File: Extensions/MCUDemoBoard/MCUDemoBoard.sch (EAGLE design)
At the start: 23 parts, among them J1 CONN_20X2NOSILK, SW1 SPST_TACT-KMR2, U1 ATSAMD21J18A-AUT, U6 MAX3232, X4 NX3215SA-32.768K-STD-MUA-8

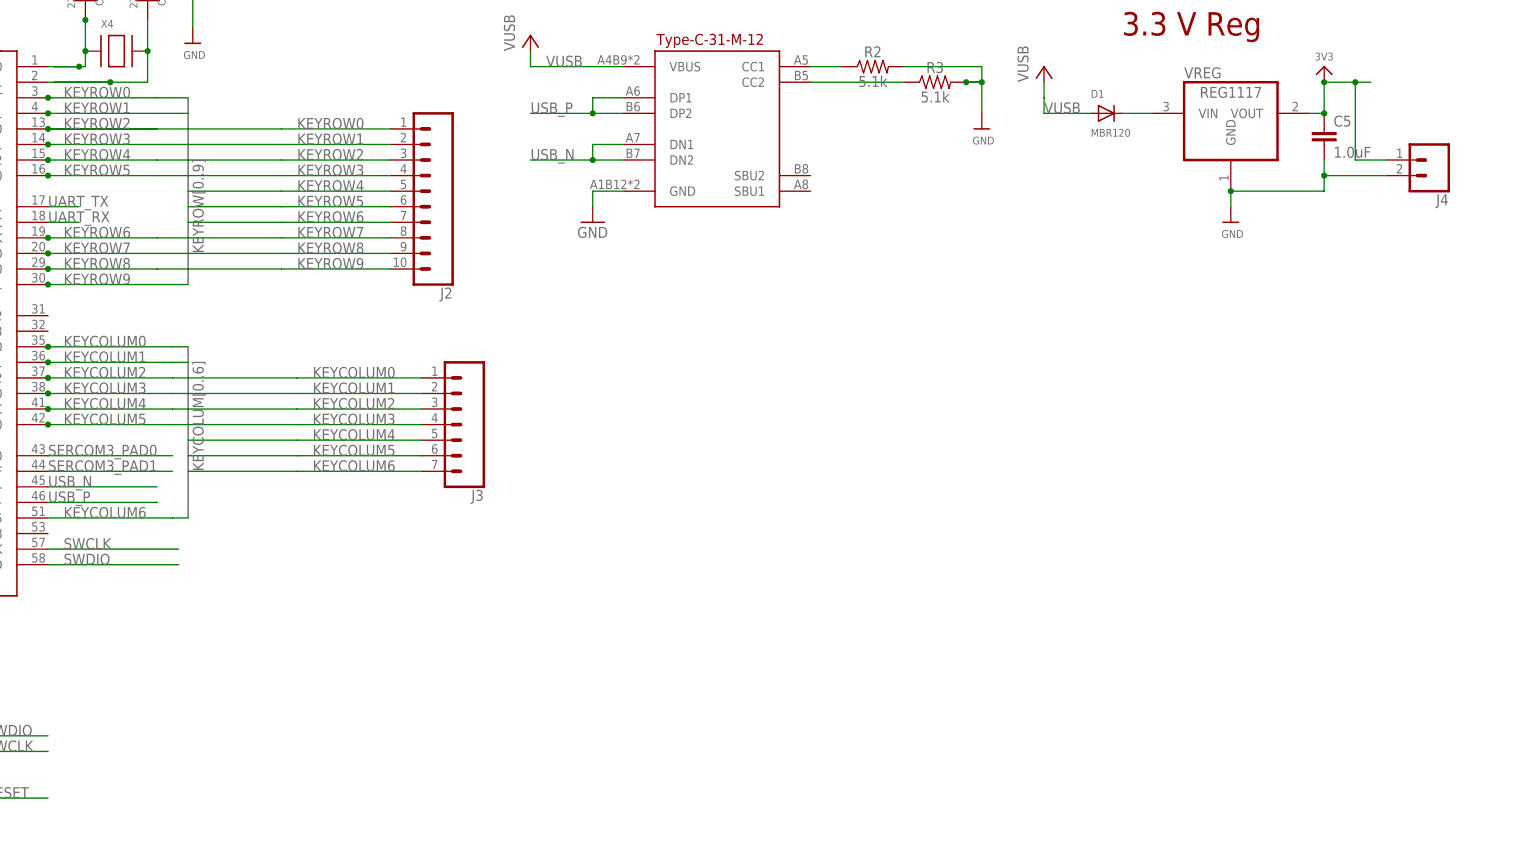
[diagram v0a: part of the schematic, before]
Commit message: changed MCU test board for FPC cable, other mods, moved test keyboard
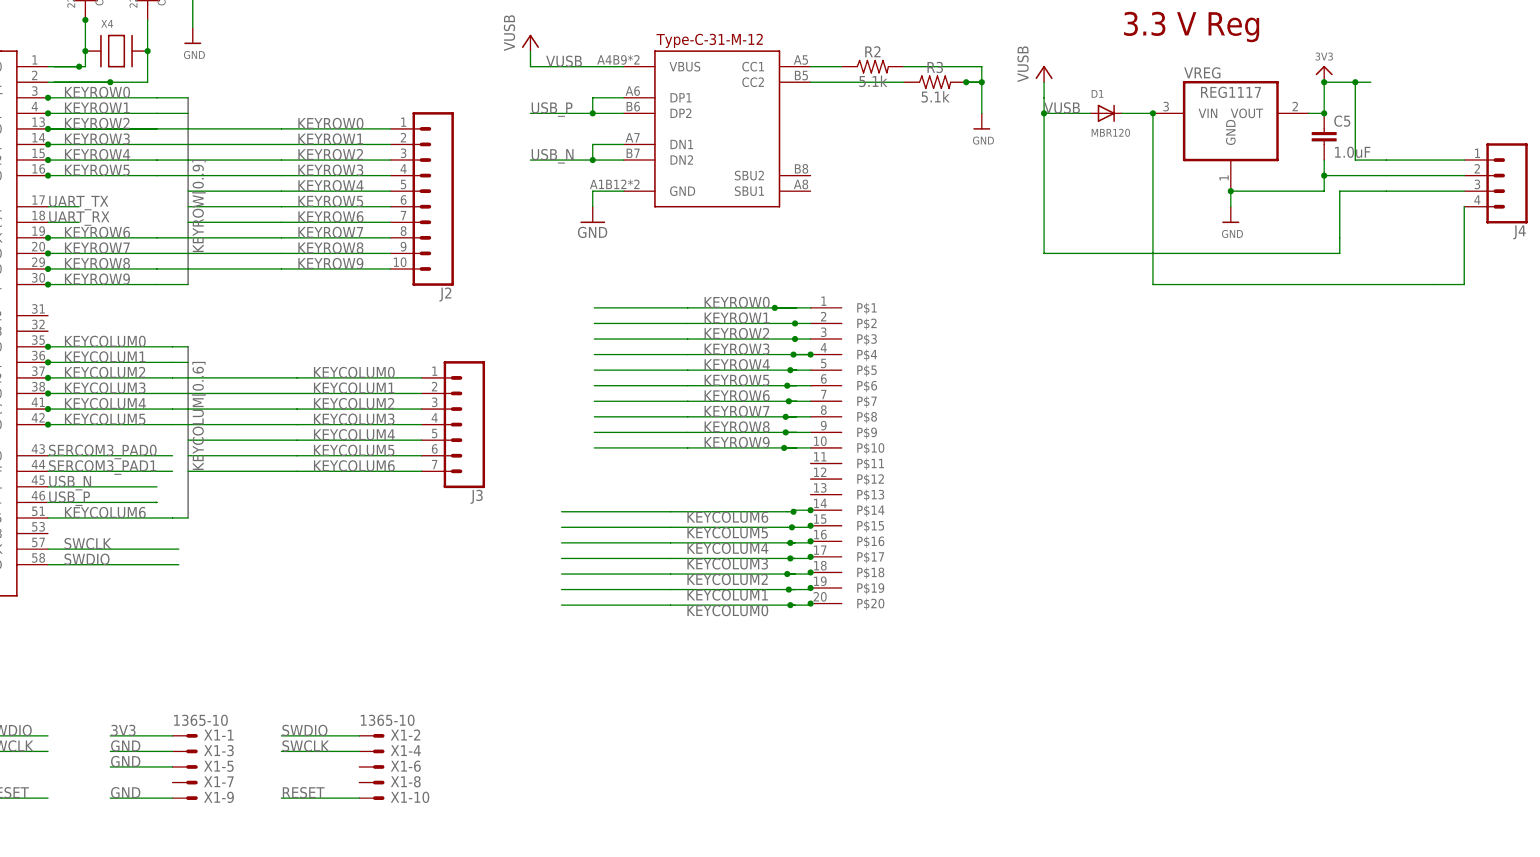
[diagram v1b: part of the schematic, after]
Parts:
- added U$1: FC1-20-L2-T-WT20PIN, FPC:FC1-20-L2-T-WT20PIN
- added X1: 1365-10, con-leotronics:1365-10
- J4: device SparkFun-Connectors:CONN_02 -> SparkFun-Connectors:CONN_04
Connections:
- net 3V3: now also X1-1.S
- net GND: now also X1-3.S, X1-5.S, X1-9.S
- net KEYCOLUM0: now also U$1.P$20
- net KEYCOLUM1: now also U$1.P$19
- net KEYCOLUM2: now also U$1.P$18
- net KEYCOLUM3: now also U$1.P$17
- net KEYCOLUM4: now also U$1.P$16
- net KEYCOLUM5: now also U$1.P$15
- net KEYCOLUM6: now also U$1.P$14
- net KEYROW0: now also U$1.P$1
- net KEYROW1: now also U$1.P$2
- net KEYROW2: now also U$1.P$3
- net KEYROW3: now also U$1.P$4
- net KEYROW4: now also U$1.P$5
- net KEYROW5: now also U$1.P$6
- net KEYROW6: now also U$1.P$7
- net KEYROW7: now also U$1.P$8
- net KEYROW8: now also U$1.P$9
- net KEYROW9: now also U$1.P$10
- net N$2: now also J4.4
- net RESET: now also X1-10.S
- net SWCLK: now also X1-4.S
- net SWDIO: now also X1-2.S
- net VUSB: now also J4.3

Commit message: Added SamD51 demo board; tried to get D51 software working
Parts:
- removed C12: 1.0uF, SparkFun-Capacitors:1.0UF-0805-25V-10%
- removed C26, C27: 22pF, SparkFun-Capacitors:1.0UF-0805-25V-10%
- removed D1: MBR120, adafruit:DIODE_SOD-123FL
- removed SW1: SPST_TACT-KMR2, adafruit:SPST_TACT-KMR2
- removed U1: ATSAMD21J18A-AUT, ATSam21:ATSAMD21J18A-AUT
- removed X4: NX3215SA-32.768K-STD-MUA-8, adafruit2:XTAL-3.2X1.5
- added C1, C2: 22pF, SparkFun-Capacitors:1.0UF-0805-25V-10%
- added C14: 10uF, microbuilder:CAP_CERAMIC0805-NOOUTLINE
- added C15: 1uF, microbuilder:CAP_CERAMIC0603_NO
- added C16, C17, C18, C19, C20, C21, C25, C28, C29, C30, C31: .1u, microbuilder:CAP_CERAMIC0603_NO
- added IC1: ATSAMD51N19A-AU, SamacSys_Parts:ATSAMD51N19A-AU
- added L3: 10uH, microbuilder:INDUCTOR
- added R15: 10K, microbuilder:RESISTOR_0603_NOOUT
- added SW2: SPST_TACT-KMR2, adafruit:SPST_TACT-KMR2
- added X2: NX3215SA-32.768K-STD-MUA-8, adafruit2:XTAL-3.2X1.5
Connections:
- removed net N$2: D1.C, J4.4, VREG.VIN
- removed net N$3: C12.1, U1.VDDCORE
- removed net N$54: C26.1, U1.PA00/EINT0/SERCOM1.0, X4.P$1
- removed net N$55: C27.1, U1.PA01/EINT1/SERCOM1.1, X4.P$2
- removed net PB31: U1.PB31
- removed net SERCOM3_PAD0: U1.PA22/I2C/I6/SERCOM3+5.0
- removed net SERCOM3_PAD1: U1.PA23/I2C/I7/SERCOM3+5.1/SOF
- new net N$26: C14.1, C15.1, C16.2, IC1.VDDCORE, L3.1
- new net N$27: IC1.VSW, L3.2
- new net N$4: C2.2, IC1.PA00, X2.P$1
- new net N$5: C1.2, IC1.PA01, X2.P$2
- net 3V3: now also C17.2, C18.2, C19.2, C20.2, C21.2, C25.2, C28.2, C29.2, C30.2, C31.2, IC1.VDDANA, IC1.VDDIOB_1, IC1.VDDIOB_2, IC1.VDDIO_1, IC1.VDDIO_2, IC1.VDDIO_3, IC1.VDDIO_4, IC1.VDDIO_5, R15.1; no longer U1.VDDA, U1.VDDIN, U1.VDDIO
- net GND: now also C1.1, C14.2, C15.2, C16.1, C17.1, C18.1, C19.1, C2.1, C20.1, C21.1, C25.1, C28.1, C29.1, C30.1, C31.1, IC1.GNDANA, IC1.GND_1, IC1.GND_2, IC1.GND_3, IC1.GND_4, IC1.GND_5, IC1.GND_6, IC1.GND_7, SW2.S, SW2.S1; no longer C12.2, C26.2, C27.2, SW1.S, SW1.S1, U1.GND, U1.GNDA
- net KEYCOLUM0: now also IC1.PC21; no longer U1.PA16/I2C/I0/SERCOM1+3.0
- net KEYCOLUM1: now also IC1.PC20; no longer U1.PA17/I2C/I1/SERCOM1+3.1
- net KEYCOLUM2: now also IC1.PC19; no longer U1.PA18/I2/SERCOM1+3.2
- net KEYCOLUM3: now also IC1.PC18; no longer U1.PA19/I3/SERCOM1+3.3/I2SD0
- net KEYCOLUM4: now also IC1.PC17; no longer U1.PA20/I4/SERCOM3+5.2/I2SSC
- net KEYCOLUM5: now also IC1.PC16; no longer U1.PA21/I5/SERCOM3/5.3/I2SFS0
- net KEYCOLUM6: now also IC1.PC15; no longer U1.PA27/I15
- net KEYROW0: now also IC1.PC14; no longer U1.PA02/EINT2/AIN0/Y0/VOUT
- net KEYROW1: now also IC1.PC13; no longer U1.PA03/EINT3/VREFA/AIN1
- net KEYROW2: now also IC1.PC12; no longer U1.PA04/EINT4/VREFB/AIN4/SERCOM0.0
- net KEYROW3: now also IC1.PC11; no longer U1.PA05/EINT5/AIN5/SERCOM0.1
- net KEYROW4: now also IC1.PC10; no longer U1.PA06/EINT6/AIN6/SSERCOM0.2
- net KEYROW5: now also IC1.PC07; no longer U1.PA07/AIN7/SERCOM0.3/I2SD0
- net KEYROW6: now also IC1.PC06; no longer U1.PA10/I10/AIN18/SERCOM0+2.2/I2SCK
- net KEYROW7: now also IC1.PC05; no longer U1.PA11/I11/AIN19/SERCOM0+2.3/I2SF0
- net KEYROW8: now also IC1.PC03; no longer U1.PA12/I12/I2C/SERCOM2+4.0
- net KEYROW9: now also IC1.PC02; no longer U1.PA13/I13/I2C/SERCOM2+4.1
- net LCD0: now also IC1.PB00; no longer U1.PB00
- net LCD1: now also IC1.PB01; no longer U1.PB01
- net LCD10: now also IC1.PB10; no longer U1.PB10
- net LCD11: now also IC1.PB11; no longer U1.PB11
- net LCD12: now also IC1.PB12; no longer U1.PB12
- net LCD13: now also IC1.PB13; no longer U1.PB13
- net LCD14: now also IC1.PB14; no longer U1.PB14
- net LCD15: now also IC1.PB15; no longer U1.PB15
- net LCD2: now also IC1.PB02; no longer U1.PB02
- net LCD3: now also IC1.PB03; no longer U1.PB03
- net LCD4: now also IC1.PB04; no longer U1.PB04
- net LCD5: now also IC1.PB05; no longer U1.PB05
- net LCD6: now also IC1.PB06; no longer U1.PB06
- net LCD7: now also IC1.PB07; no longer U1.PB07
- net LCD8: now also IC1.PB08; no longer U1.PB08
- net LCD9: now also IC1.PB09; no longer U1.PB09
- net LCD_CS: now also IC1.PB22; no longer U1.PB22
- net LCD_D/C: now also IC1.PB23; no longer U1.PB23
- net LCD_RD: now also IC1.PB16; no longer U1.PB16
- net LCD_RESET: now also IC1.PB30; no longer U1.PB30
- net LCD_W/R: now also IC1.PB17; no longer U1.PB17
- net RESET: now also IC1.RESETN, R15.2, SW2.P, SW2.P1; no longer SW1.P, SW1.P1, U1./RESET
- net SWCLK: now also IC1.PA30; no longer U1.PA30/I10/SECOM1.2/SWCLK
- net SWDIO: now also IC1.PA31; no longer U1.PA31/I11/SECOM1.3/SWDIO
- net UART_RX: now also IC1.PA09; no longer U1.PA09/I2C/I9/AIN17/SERCOM0+2.1/I2SMC
- net UART_TX: now also IC1.PA08; no longer U1.PA08/I2C/AIN16/SERCOM0+2.0/I2SD1
- net USB_N: now also IC1.PA24; no longer U1.PA24/I12/SERCOM3+5.2/D-
- net USB_P: now also IC1.PA25; no longer U1.PA25/I13/SERCOM3+5.3/D+
- net VUSB: now also J4.4, VREG.VIN; no longer D1.A
